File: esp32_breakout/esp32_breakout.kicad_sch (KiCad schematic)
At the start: 25 parts, among them J1 JST B5B-PH-K-S, J10 JST B6B-ZR, J2 JST B5B-PH-K-S, J3 JST B6B-PH-K-S, J4 XT30U-M, J5 HDR M VERT 12p 2.54mm, J9 JST B6B-ZR, SW1 SS12D10, U1 ESP32 DEV KIT Module 30-pin, U2 LM2596 Module

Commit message: Schematic notes
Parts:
- removed J1, J2: JST B5B-PH-K-S, Connector_JST:JST_PH_B5B-PH-K_1x05_P2.00mm_Vertical, symbol Connector_Generic:Conn_01x05
- removed J5: HDR M VERT 12p 2.54mm, Connector_PinSocket_2.54mm:PinSocket_1x12_P2.54mm_Vertical, symbol Connector_Generic:Conn_01x12
- added J1, J2: JST B7B-PH-K-S, Connector_JST:JST_PH_B7B-PH-K_1x07_P2.00mm_Vertical, symbol Connector_Generic:Conn_01x07
- added J6: JST B5B-PH-K-S, Connector_JST:JST_PH_B5B-PH-K_1x05_P2.00mm_Vertical, symbol Connector_Generic:Conn_01x05
- added J7: DNP HDR M VERT 6P 2.54mm, Connector_PinSocket_2.54mm:PinSocket_1x06_P2.54mm_Vertical, symbol Connector_Generic:Conn_01x06
- added R6, R7: 10k, Resistor_SMD:R_0603_1608Metric, symbol Device:R_Small_US
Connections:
- net +3V3: now also J7.2 (Pin_2)
- net +5V: now also J1.7 (Pin_7), J2.7 (Pin_7), J6.1 (Pin_1), J7.1 (Pin_1)
- net GND: now also J1.2 (Pin_2), J2.2 (Pin_2), J6.4 (Pin_4), J6.5 (Pin_5), J7.3 (Pin_3)
- net GPIO12_OUT_STRAP: now also J6.2 (Pin_2)
- net GPIO27_TOUCH: now also J7.4 (Pin_4)
- net GPIO4_TOUCH: now also J7.5 (Pin_5)
- net GPIO5_BOOT_STRAP: now also J7.6 (Pin_6)
- net MOT_FG_LEFT: now also U1.20 (RTC_GPIO5/ADC1_CH7/GPIO35_IN); no longer R3.1
- net Vdrive: now also J1.5 (Pin_5), J2.5 (Pin_5)
- net at R3.2: now also J2.4 (Pin_4)
- net at R4.2: now also J1.4 (Pin_4)
- net at R5.2: now also J6.3 (Pin_3)
- net GPIO26_TOUCH renamed ENC_B_RIGHT
- net ENC_B_RIGHT: now also R7.1
- net GPIO32_TOUCH renamed ENC_B_LEFT
- net ENC_B_LEFT: now also R6.1
- net MOT_FG_RIGHT renamed MOT_FG_RIGHT_ENC_A
- net MOT_FG_RIGHT_ENC_A: no longer U1.20 (RTC_GPIO5/ADC1_CH7/GPIO35_IN)
- new net: J2.6 (Pin_6), R6.2
- new net: J1.6 (Pin_6), R7.2
- new net MOT_CW_LEFT_IN2: J2.3 (Pin_3)
- new net MOT_CW_RIGHT_IN4: J1.3 (Pin_3)
- new net MOT_FG_LEFT_ENC_A: R3.1
- new net MOT_PWM_LEFT_IN1: J2.1 (Pin_1)
- new net MOT_PWM_RIGHT_IN3: J1.1 (Pin_1)
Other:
- note added: "9..24V"
- note added: "SPARE GPIO, SONAR"
- note added: "VCC 5V Trig/Tx Echo/Rx GND GND"
- note removed: "24V or 12V"
- note removed: "GND GND Echo/Rx Trig/Tx VCC 5V"
- note removed: "GPIO, SONAR US-100"
- moved on the sheet: R3, R4

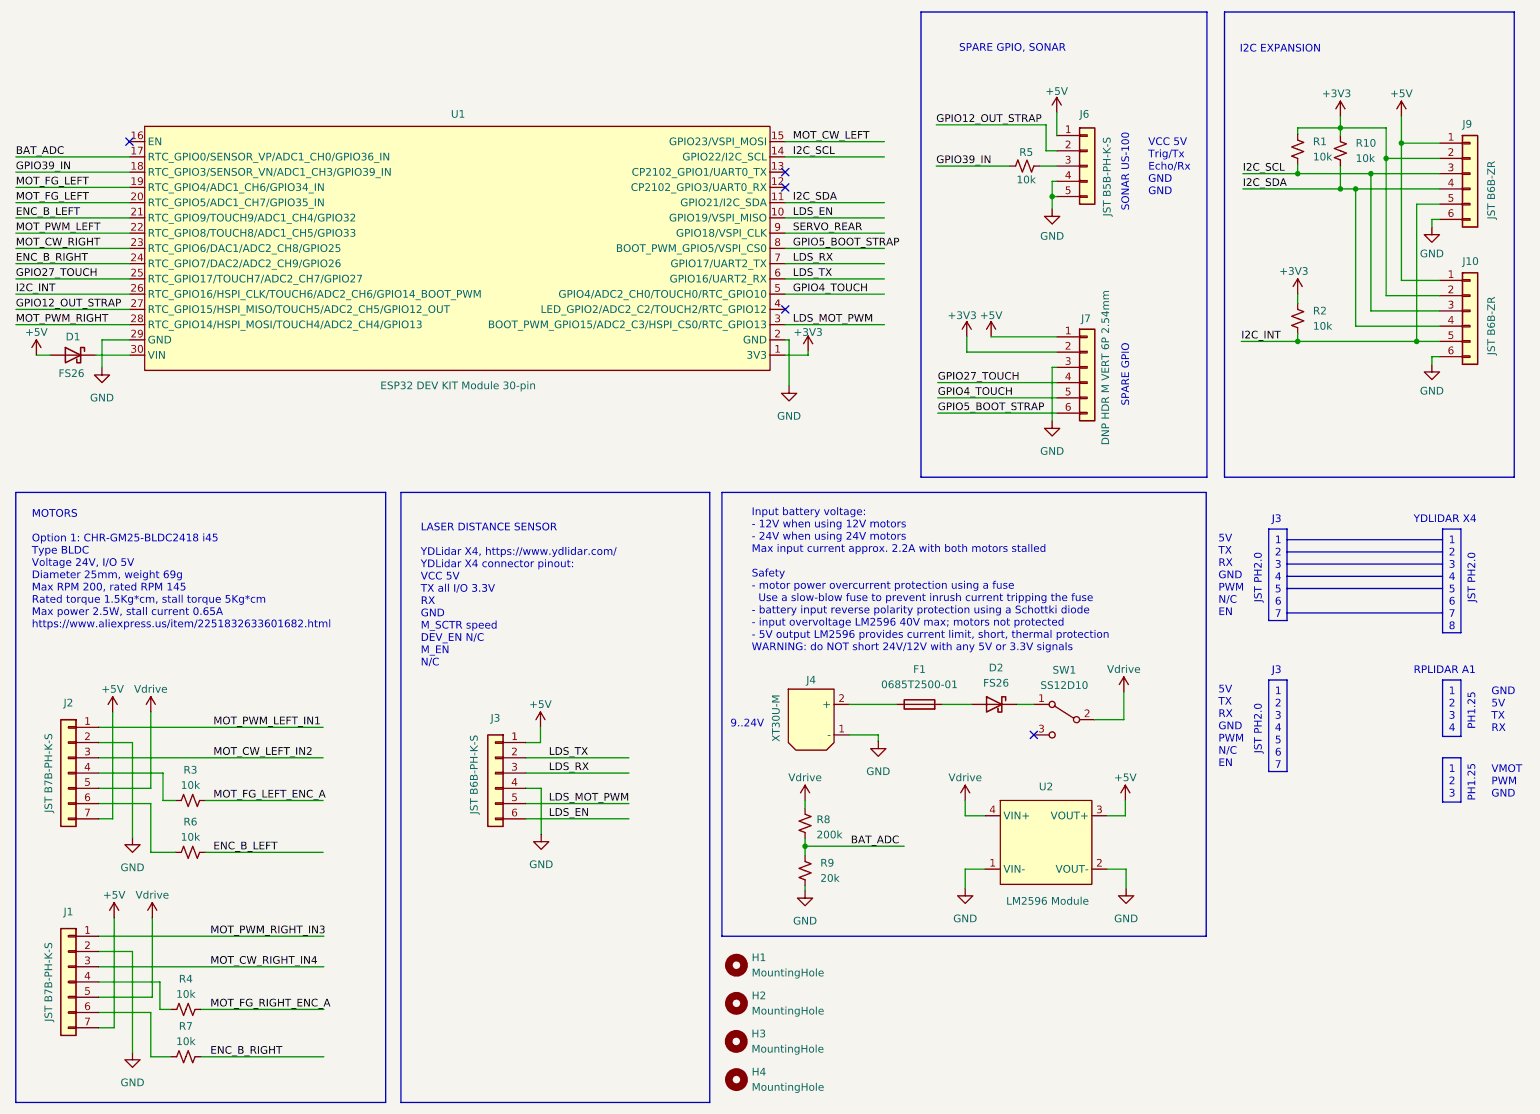
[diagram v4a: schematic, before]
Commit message: Brushed, quad-encoder motors
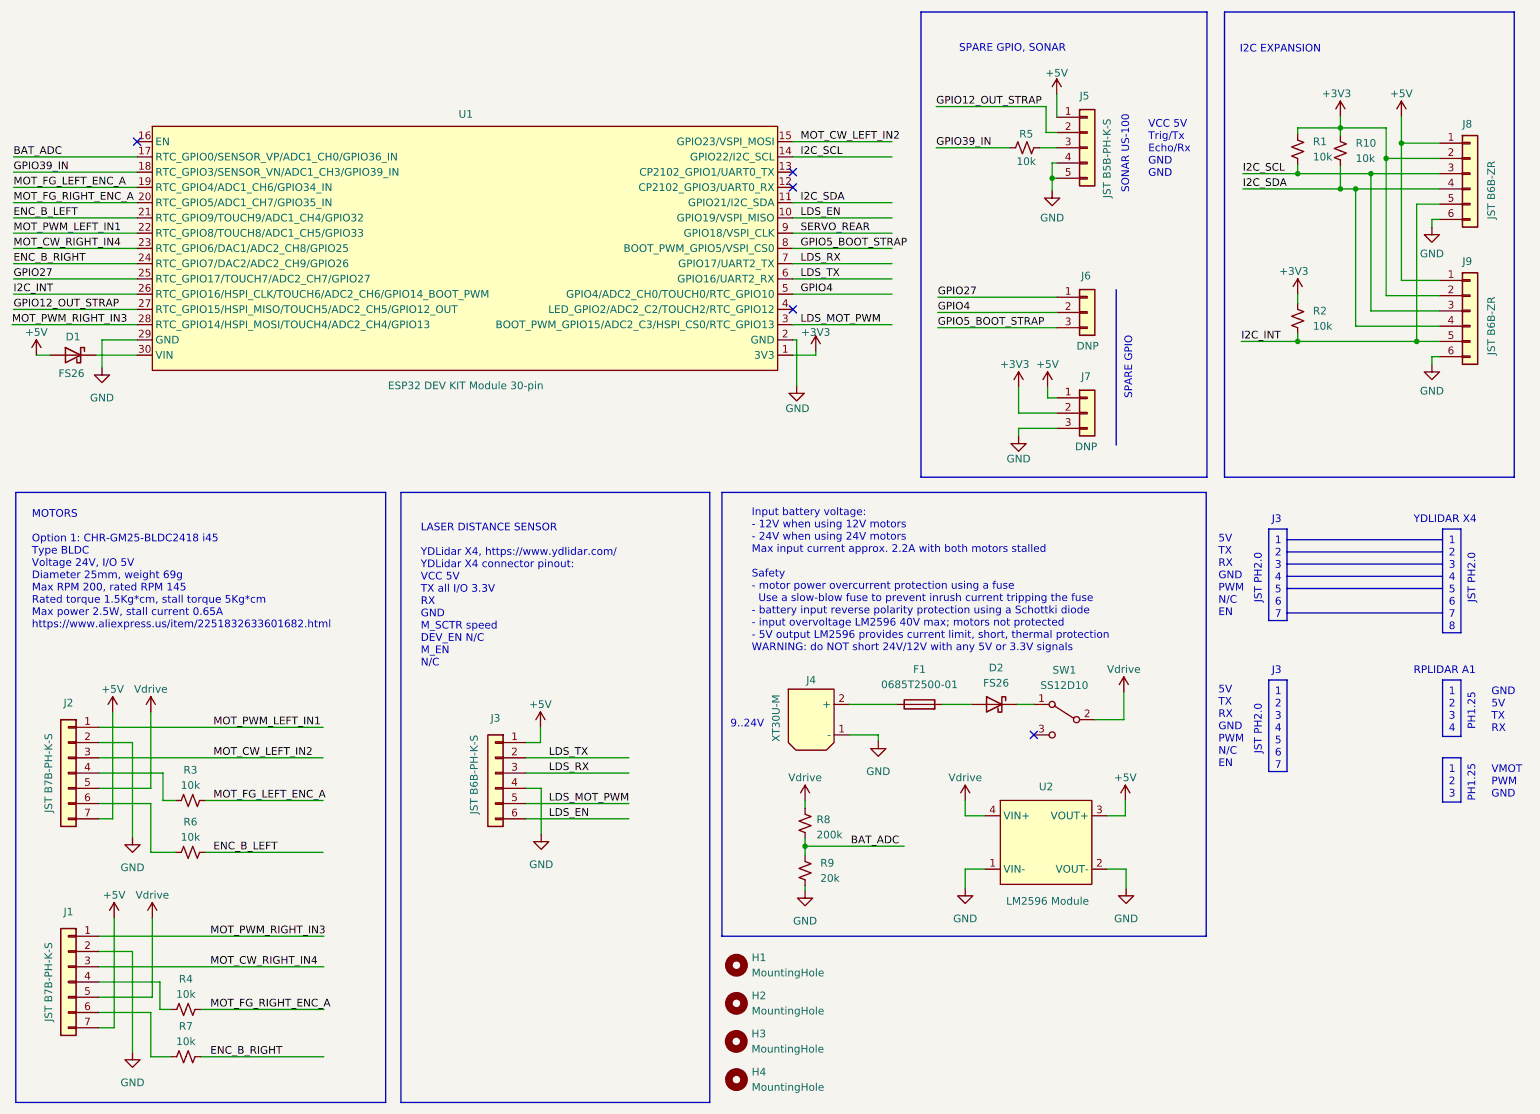
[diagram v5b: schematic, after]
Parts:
- removed J7: DNP HDR M VERT 6P 2.54mm, Connector_PinSocket_2.54mm:PinSocket_1x06_P2.54mm_Vertical, symbol Connector_Generic:Conn_01x06
- added J6, J7: DNP, Connector_PinSocket_2.54mm:PinSocket_1x03_P2.54mm_Vertical, symbol Connector_Generic:Conn_01x03
- renumbered J6 to J5, J9 to J8, J10 to J9
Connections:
- net MOT_CW_LEFT is gone; now on net MOT_CW_LEFT_IN2: U1.15 (GPIO23/VSPI_MOSI)
- net MOT_CW_RIGHT is gone; now on net MOT_CW_RIGHT_IN4: U1.23 (RTC_GPIO6/DAC1/ADC2_CH8/GPIO25)
- net MOT_PWM_LEFT is gone; now on net MOT_PWM_LEFT_IN1: U1.22 (RTC_GPIO8/TOUCH8/ADC1_CH5/GPIO33)
- net MOT_PWM_RIGHT is gone; now on net MOT_PWM_RIGHT_IN3: U1.28 (RTC_GPIO14/HSPI_MOSI/TOUCH4/ADC2_CH4/GPIO13)
- net +3V3: now also J7.2 (Pin_2)
- net +5V: now also J7.1 (Pin_1)
- net GND: now also J7.3 (Pin_3)
- net GPIO5_BOOT_STRAP: now also J6.3 (Pin_3)
- net MOT_FG_LEFT_ENC_A: now also U1.19 (RTC_GPIO4/ADC1_CH6/GPIO34_IN)
- net MOT_FG_RIGHT_ENC_A: now also U1.20 (RTC_GPIO5/ADC1_CH7/GPIO35_IN)
- net GPIO27_TOUCH renamed GPIO27
- net GPIO27: now also J6.1 (Pin_1)
- net GPIO4_TOUCH renamed GPIO4
- net GPIO4: now also J6.2 (Pin_2)
- removed net MOT_FG_LEFT: U1.19 (RTC_GPIO4/ADC1_CH6/GPIO34_IN), U1.20 (RTC_GPIO5/ADC1_CH7/GPIO35_IN)
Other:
- moved on the sheet: J5, R5, U1

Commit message: ZH connectors
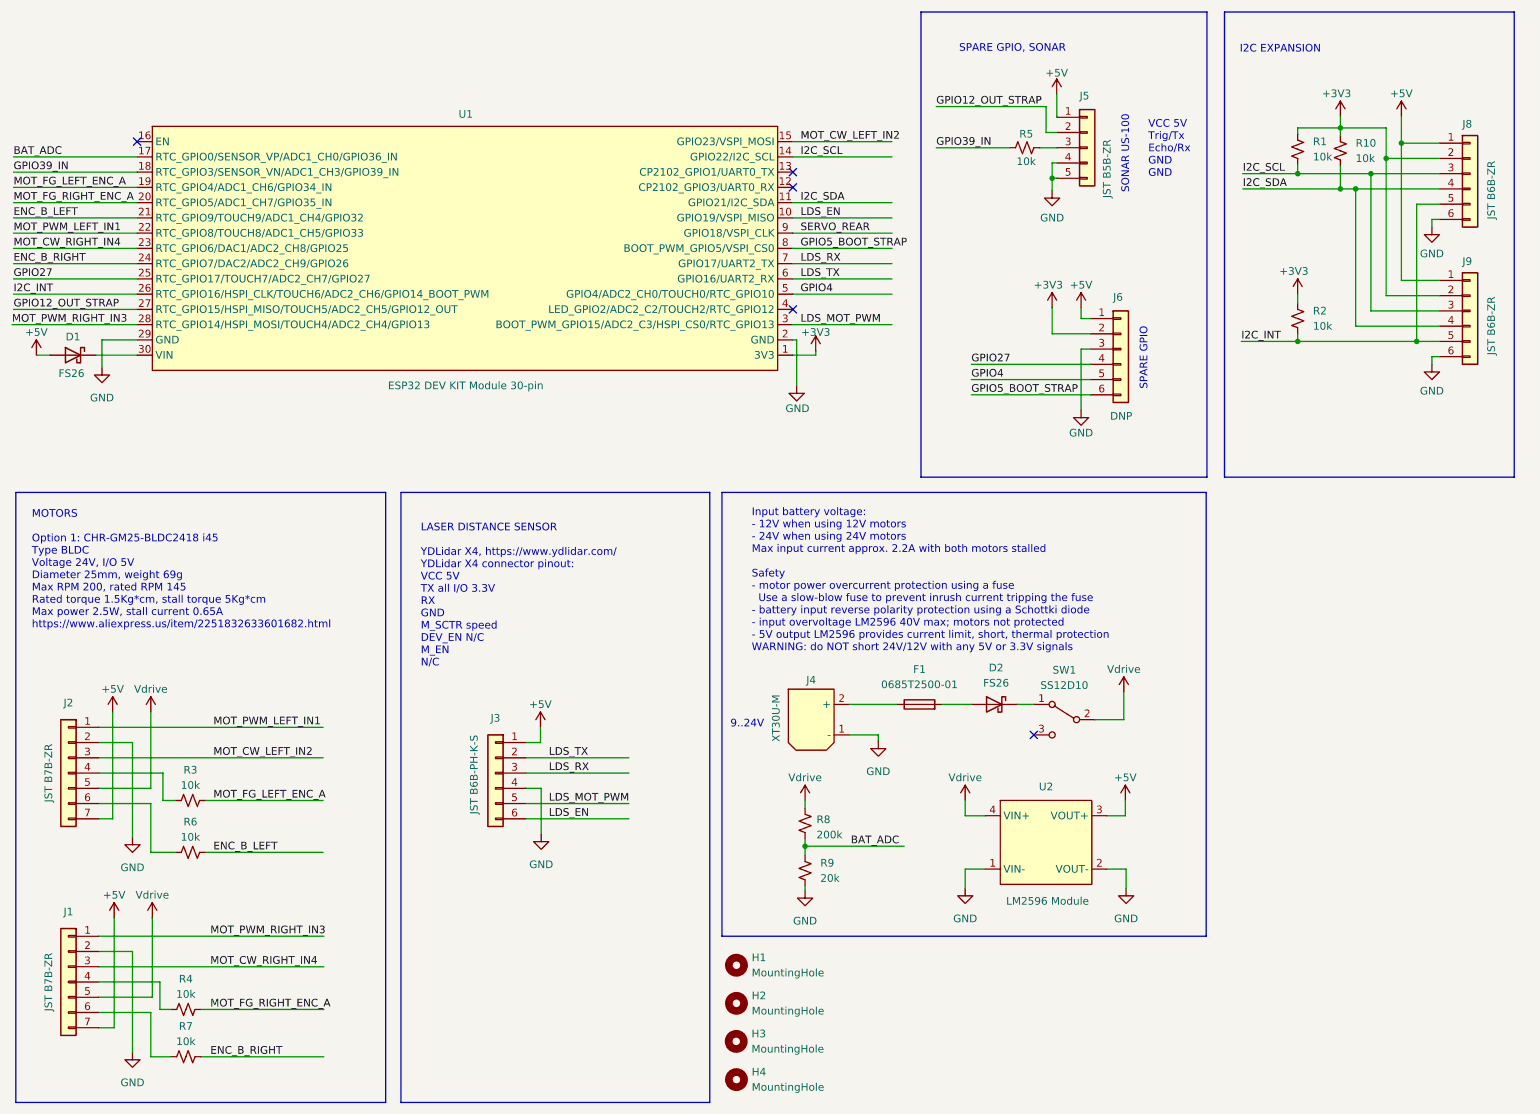
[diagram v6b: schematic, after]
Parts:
- removed J6, J7: DNP, Connector_PinSocket_2.54mm:PinSocket_1x03_P2.54mm_Vertical, symbol Connector_Generic:Conn_01x03
- added J6: DNP, Connector_PinSocket_2.54mm:PinSocket_1x06_P2.54mm_Vertical, symbol Connector_Generic:Conn_01x06
- J1, J2: value JST B7B-PH-K-S -> JST B7B-ZR; footprint Connector_JST:JST_PH_B7B-PH-K_1x07_P2.00mm_Vertical -> Makerspet:JST_ZH_B7B-ZR_1x07_P1.50mm_Vertical
- J5: value JST B5B-PH-K-S -> JST B5B-ZR; footprint Connector_JST:JST_PH_B5B-PH-K_1x05_P2.00mm_Vertical -> Makerspet:JST_ZH_B5B-ZR_1x05_P1.50mm_Vertical
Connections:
- net +3V3: now also J6.2 (Pin_2)
- net +5V: now also J6.1 (Pin_1)
- net GND: now also J6.3 (Pin_3)
- net GPIO27: now also J6.4 (Pin_4)
- net GPIO4: now also J6.5 (Pin_5)
- net GPIO5_BOOT_STRAP: now also J6.6 (Pin_6)
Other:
- note removed: "5V TX RX GND PWM N/C EN"
- note removed: "GND 5V TX RX"
- note removed: "J3"
- note removed: "JST PH2.0"
- note removed: "PH1.25"
- note removed: "RPLIDAR A1"
- note removed: "VMOT PWM GND"
- note removed: "YDLIDAR X4"
